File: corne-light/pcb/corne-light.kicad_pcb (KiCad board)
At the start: 2 copper layers, 275.5 x 105.6 mm, 122 parts, among them J1 MJ-4PP-9, J2 OLED, J5 Breakaway_Tabs, J6 MJ-4PP-9, J7 OLED, SW1 SW_PUSH, SW10 SW_PUSH, SW11 SW_PUSH, SW12 SW_PUSH, SW13 SW_PUSH, SW14 SW_PUSH, SW15 SW_PUSH, SW16 SW_PUSH, SW17 SW_PUSH, SW18 SW_PUSH, SW19 SW_PUSH, SW2 SW_PUSH, SW20 SW_PUSH, SW21 SW_PUSH, SW22 SW_PUSH, SW23 SW_PUSH, SW24 SW_PUSH, SW25 SW_PUSH, SW26 SW_PUSH, SW27 SW_PUSH, SW28 SW_PUSH, SW29 SW_PUSH, SW3 SW_PUSH, SW30 SW_PUSH, SW31 SW_PUSH, SW32 SW_PUSH, SW33 SW_PUSH, SW34 SW_PUSH, SW35 SW_PUSH, SW36 SW_PUSH, SW37 SW_PUSH, SW38 SW_PUSH, SW39 SW_PUSH, SW4 SW_PUSH, SW40 SW_PUSH, SW41 SW_PUSH, SW42 SW_PUSH, SW5 SW_PUSH, SW6 SW_PUSH, SW7 SW_PUSH, SW8 SW_PUSH, SW9 SW_PUSH, U1 ProMicro, U2 ProMicro

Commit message: Change switches to redragon ones
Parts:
- removed G*** (x4): LOGO, kbd:corne-logo-horizontal
- removed J1, J6: MJ-4PP-9, kbd:MJ-4PP-9_1side
- removed J5 (x8): Breakaway_Tabs, kbd:Breakaway_Tabs
- removed Ref** (x4): Val**, kbd:thread_m2
- removed Ref** (x14): Val**, kbd:spacer_m2
- D1, D10, D11, D12, D13, D14, D15, D16, D17, D18, D19, D2, D20, D21, D22, D23, D24, D25, D26, D27, D28, D29, D3, D30, D31, D32, D33, D34, D35, D36, D37, D38, D39, D4, D40, D41, D42, D5, D6, D7, D8, D9: footprint kbd:D3_TH_SMD_v2 -> kbd:D3_TH
- SW1, SW10, SW11, SW12, SW13, SW14, SW15, SW16, SW17, SW18, SW19, SW2, SW20, SW22, SW23, SW24, SW25, SW26, SW27, SW28, SW29, SW3, SW30, SW31, SW32, SW33, SW34, SW35, SW36, SW37, SW38, SW39, SW4, SW40, SW41, SW5, SW6, SW7, SW8, SW9: footprint kbd:keyswitch_cherrymx_alps_choc12_1u -> ProjectLocal:SW_Redragon_LowProfile_PCB_1.00u
- SW21, SW42: footprint kbd:keyswitch_cherrymx_alps_choc12_1.5u -> ProjectLocal:SW_Redragon_LowProfile_PCB_1.50u
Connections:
- U1 pad 1: Net-(U1-Pad1) -> unconnected-(U1-TX0/D3-Pad1)
- U1 pad 11: Net-(U1-Pad11) -> unconnected-(U1-8/B4-Pad11)
- U1 pad 12: Net-(U1-Pad12) -> unconnected-(U1-9/B5-Pad12)
- U1 pad 13: Net-(U1-Pad13) -> unconnected-(U1-B6/10-Pad13)
- U1 pad 14: Net-(U1-Pad14) -> unconnected-(U1-B2/16-Pad14)
- U1 pad 2: data -> unconnected-(U1-RX1/D2-Pad2)
- U1 pad 24: Net-(U1-Pad24) -> unconnected-(U1-RAW-Pad24)
- U2 pad 1: Net-(U2-Pad1) -> unconnected-(U2-TX0/D3-Pad1)
- U2 pad 11: Net-(U2-Pad11) -> unconnected-(U2-8/B4-Pad11)
- U2 pad 12: Net-(U2-Pad12) -> unconnected-(U2-9/B5-Pad12)
- U2 pad 13: Net-(U2-Pad13) -> unconnected-(U2-B6/10-Pad13)
- U2 pad 14: Net-(U2-Pad14) -> unconnected-(U2-B2/16-Pad14)
- U2 pad 2: data_r -> unconnected-(U2-RX1/D2-Pad2)
- U2 pad 24: Net-(U2-Pad24) -> unconnected-(U2-RAW-Pad24)
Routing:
- net (no net): track 0.00 -> 528.0 mm
- net unconnected-(U1-RX1/D2-Pad2): track 0.00 -> 78.9 mm
- net data: track 78.9 -> 0.00 mm
- net unconnected-(U2-RX1/D2-Pad2): track 0.00 -> 64.4 mm
- net data_r: track 64.4 -> 0.00 mm
- net Net-(D16-A): track 35.7 -> 0.00 mm
- net Net-(D27-A): track 20.5 -> 6.93 mm
- net Net-(D33-A): track 20.5 -> 6.99 mm
- net Net-(D23-A): track 21.5 -> 8.01 mm
- net Net-(D31-A): track 22.6 -> 9.12 mm
- net Net-(D37-A): track 22.3 -> 8.84 mm
- net Net-(D24-A): track 27.6 -> 14.2 mm
- net Net-(D36-A): track 27.2 -> 13.8 mm
- net Net-(D25-A): track 22.3 -> 8.90 mm
- net Net-(D32-A): track 27.5 -> 14.1 mm
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
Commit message: Change diode orientation on right side
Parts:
- D1, D10, D11, D12, D13, D14, D15, D16, D17, D18, D19, D2, D20, D21, D22, D23, D24, D25, D26, D27, D28, D29, D3, D30, D31, D32, D33, D34, D35, D36, D37, D38, D39, D4, D40, D41, D42, D5, D6, D7, D8, D9: footprint kbd:D3_TH -> Diode_THT:D_DO-35_SOD27_P12.70mm_Horizontal
- moved D42 33.6 mm to (170.8, 84.5), turned to 180 degrees
- moved D24 21.5 mm to (250.5, 53.0)
- moved D30 21.5 mm to (250.5, 72.0)
- moved D36 21.5 mm to (250.5, 91.0)
- moved D26 20.2 mm to (212.0, 51.4)
- moved D32 20.2 mm to (212.0, 70.3)
- moved D38 20.2 mm to (212.0, 89.3)
- moved D27 10.5 mm to (193.0, 51.4)
- moved D33 10.5 mm to (193.0, 70.3)
- moved D39 10.5 mm to (193.0, 89.3)
- moved D37 10.4 mm to (229.7, 89.3)
- moved D25 10.4 mm to (229.7, 51.3)
- moved D31 10.4 mm to (229.7, 70.3)
- moved D40 7.02 mm to (222.0, 92.2), turned to -90 degrees
- moved D41 6.64 mm to (202.0, 92.7), turned to -90 degrees
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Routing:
- net (no net): track 528.0 -> 0.00 mm
- net col0_r: track 183.2 -> 0.00 mm, vias 1 -> 0
- net col0: track 182.3 -> 0.00 mm, vias 1 -> 0
- net row1: track 164.0 -> 0.00 mm
- net col1_r: track 161.3 -> 0.00 mm
- net col1: track 156.5 -> 0.00 mm, vias 1 -> 0
- net row2: track 153.9 -> 0.00 mm
- net col3_r: track 148.5 -> 0.00 mm, vias 1 -> 0
- net row0: track 142.3 -> 0.00 mm
- net col3: track 141.3 -> 0.00 mm, vias 1 -> 0
- net col2_r: track 141.1 -> 0.00 mm, vias 1 -> 0
- net row2_r: track 137.6 -> 0.00 mm, vias 2 -> 0
- net col2: track 135.2 -> 0.00 mm, vias 1 -> 0
- net row1_r: track 134.3 -> 0.00 mm
- net col4_r: track 129.6 -> 0.00 mm, vias 1 -> 0
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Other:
- outline, holes or cut-outs redrawn

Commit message: Route rightside keys
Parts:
- removed D1, D10, D11, D12, D13, D14, D15, D16, D17, D18, D19, D2, D20, D21, D3, D4, D5, D6, D7, D8, D9: D, Diode_THT:D_DO-35_SOD27_P12.70mm_Horizontal
- removed J2, J7: OLED, kbd:OLED_1side
- removed RSW1, RSW2: SW_PUSH, kbd:ResetSW_1side
- removed SW1, SW10, SW11, SW12, SW13, SW14, SW15, SW16, SW17, SW18, SW19, SW2, SW20, SW3, SW4, SW5, SW6, SW7, SW8, SW9: SW_PUSH, ProjectLocal:SW_Redragon_LowProfile_PCB_1.00u
- removed SW21: SW_PUSH, ProjectLocal:SW_Redragon_LowProfile_PCB_1.50u
- removed U2: ProMicro, kbd:ProMicro_v3
- D22, D23, D24, D25, D26, D27, D28, D29, D30, D31, D32, D33, D34, D35, D36, D37, D38, D39, D40, D41, D42: footprint Diode_THT:D_DO-35_SOD27_P12.70mm_Horizontal -> Diode_THT:D_DO-35_SOD27_P10.16mm_Horizontal; moved to F.Cu
- U1: value ProMicro -> nice_nano; footprint kbd:ProMicro_v3 -> PCM_marbastlib-xp-promicroish:nice_nano_AH_USBup
- moved D30 28.4 mm to (231.4, 51.0), turned to 0 degrees
- moved D36 28.0 mm to (230.9, 71.0), turned to 0 degrees
- moved D31 27.5 mm to (212.4, 49.0), turned to 0 degrees
- moved D37 27.4 mm to (211.9, 68.5), turned to 0 degrees
- moved U1 27.2 mm to (164.1, 56.2)
- moved D32 26.5 mm to (193.9, 51.0), turned to 0 degrees
- moved D38 24.8 mm to (195.9, 70.5), turned to 0 degrees
- moved D39 23.1 mm to (179.0, 71.0), turned to 0 degrees
- moved D29 22.4 mm to (250.4, 56.0), turned to 0 degrees
- moved D35 22.1 mm to (250.4, 75.5), turned to 0 degrees
- moved D33 22.0 mm to (179.5, 53.0), turned to 0 degrees
- moved D24 20.5 mm to (231.2, 45.8)
- moved D27 20.4 mm to (175.5, 61.9)
- moved D26 18.2 mm to (194.0, 48.5)
- moved D25 17.9 mm to (212.5, 46.5)
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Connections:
- D22 pad 1: row0_r -> col0_r
- D23 pad 1: row0_r -> col1_r
- D24 pad 1: row0_r -> col2_r
- D25 pad 1: row0_r -> col3_r
- D26 pad 1: row0_r -> col4_r
- D27 pad 1: row0_r -> col5_r
- D28 pad 1: row1_r -> col0_r
- D29 pad 1: row1_r -> col1_r
- D30 pad 1: row1_r -> col2_r
- D31 pad 1: row1_r -> col3_r
- D32 pad 1: row1_r -> col4_r
- D33 pad 1: row1_r -> col5_r
- D34 pad 1: row2_r -> col0_r
- D35 pad 1: row2_r -> col1_r
- D36 pad 1: row2_r -> col2_r
- D37 pad 1: row2_r -> col3_r
- D38 pad 1: row2_r -> col4_r
- D39 pad 1: row2_r -> col5_r
- D40 pad 1: row3_r -> col3_r
- D41 pad 1: row3_r -> col4_r
- D42 pad 1: row3_r -> col5_r
- SW22 pad 1: col0_r -> Net-(D22-A)
- SW22 pad 2: Net-(D22-A) -> row0_r
- SW23 pad 1: col1_r -> Net-(D23-A)
- SW23 pad 2: Net-(D23-A) -> row0_r
- SW24 pad 1: col2_r -> Net-(D24-A)
- SW24 pad 2: Net-(D24-A) -> row0_r
- SW25 pad 1: col3_r -> Net-(D25-A)
- SW25 pad 2: Net-(D25-A) -> row0_r
- SW26 pad 1: col4_r -> Net-(D26-A)
- SW26 pad 2: Net-(D26-A) -> row0_r
- SW27 pad 1: col5_r -> Net-(D27-A)
- SW27 pad 2: Net-(D27-A) -> row0_r
- SW28 pad 1: col0_r -> Net-(D28-A)
- SW28 pad 2: Net-(D28-A) -> row1_r
- SW29 pad 1: col1_r -> Net-(D29-A)
- SW29 pad 2: Net-(D29-A) -> row1_r
- SW30 pad 1: col2_r -> Net-(D30-A)
- SW30 pad 2: Net-(D30-A) -> row1_r
- SW31 pad 1: col3_r -> Net-(D31-A)
- SW31 pad 2: Net-(D31-A) -> row1_r
- SW32 pad 1: col4_r -> Net-(D32-A)
- SW32 pad 2: Net-(D32-A) -> row1_r
- SW33 pad 1: col5_r -> Net-(D33-A)
- SW33 pad 2: Net-(D33-A) -> row1_r
- SW34 pad 1: col0_r -> Net-(D34-A)
- SW34 pad 2: Net-(D34-A) -> row2_r
- SW35 pad 1: col1_r -> Net-(D35-A)
- SW35 pad 2: Net-(D35-A) -> row2_r
- SW36 pad 1: col2_r -> Net-(D36-A)
- SW36 pad 2: Net-(D36-A) -> row2_r
- SW37 pad 1: col3_r -> Net-(D37-A)
- SW37 pad 2: Net-(D37-A) -> row2_r
- SW38 pad 1: col4_r -> Net-(D38-A)
- SW38 pad 2: Net-(D38-A) -> row2_r
- SW39 pad 1: col5_r -> Net-(D39-A)
- SW39 pad 2: Net-(D39-A) -> row2_r
- SW40 pad 1: col3_r -> Net-(D40-A)
- SW40 pad 2: Net-(D40-A) -> row3_r
- SW41 pad 1: col4_r -> Net-(D41-A)
- SW41 pad 2: Net-(D41-A) -> row3_r
- SW42 pad 1: col5_r -> Net-(D42-A)
- SW42 pad 2: Net-(D42-A) -> row3_r
- U1 pad 10: row3 -> col4_r
- U1 pad 11: unconnected-(U1-8/B4-Pad11) -> col3_r
- U1 pad 12: unconnected-(U1-9/B5-Pad12) -> row3_r
- U1 pad 15: col5 -> unconnected-(U1-RST-Pad15)
- U1 pad 16: col4 -> unconnected-(U1-3V3-Pad16)
- U1 pad 17: col3 -> col0_r
- U1 pad 18: col2 -> col1_r
- U1 pad 19: col1 -> col2_r
- U1 pad 20: col0 -> unconnected-(U1-P1.15-LF-Pad20)
- U1 pad 21: VCC -> unconnected-(U1-P1.13-LF-Pad21)
- U1 pad 22: reset -> col5_r
- U1 pad 23: GND -> unconnected-(U1-P0.10-LF-Pad23)
- U1 pad 3: GND -> unconnected-(U1-GND-Pad3)
- U1 pad 4: GND -> unconnected-(U1-GND-Pad4)
- U1 pad 5: SDA -> unconnected-(U1-P0.17-Pad5)
- U1 pad 6: SCL -> unconnected-(U1-P0.20-Pad6)
- U1 pad 7: row0 -> row0_r
- U1 pad 8: row1 -> row1_r
- U1 pad 9: row2 -> row2_r
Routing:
- net row0_r: track 0.00 -> 343.2 mm
- net row2_r: track 0.00 -> 314.3 mm
- net row1_r: track 0.00 -> 286.6 mm
- net col0_r: track 0.00 -> 149.2 mm
- net col3_r: track 0.00 -> 136.1 mm
- net col1_r: track 0.00 -> 124.7 mm
- net col4_r: track 0.00 -> 115.2 mm
- net row3_r: track 0.00 -> 97.9 mm
- net col2_r: track 0.00 -> 92.8 mm
- net col5_r: track 0.00 -> 59.5 mm
- net Net-(D42-A): track 0.00 -> 26.2 mm
- net Net-(D23-A): track 0.00 -> 20.3 mm
- net Net-(D24-A): track 0.00 -> 20.0 mm
- net Net-(D25-A): track 0.00 -> 19.7 mm
- net Net-(D26-A): track 0.00 -> 19.2 mm
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
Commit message: Improve  routing
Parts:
- moved D27 3.48 mm to (175.1, 65.3)
- moved D41 0.98 mm to (195.9, 89.0)
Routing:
- net col2_r: track 92.8 -> 102.2 mm
- net row1_r: track 286.6 -> 292.8 mm
- net col5_r: track 59.5 -> 53.9 mm
- net row0_r: track 343.2 -> 347.4 mm
- net Net-(D27-A): track 14.5 -> 18.1 mm
- net row2_r: track 314.3 -> 316.0 mm
- net Net-(D42-A): track 26.2 -> 27.9 mm
- net row3_r: track 97.9 -> 96.8 mm
- net col4_r: track 115.2 -> 114.5 mm
- net col3_r: track 136.1 -> 135.5 mm
- net col1_r: track 124.7 -> 124.1 mm

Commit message: Improve tracks
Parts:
- D27, D33: footprint Diode_THT:D_DO-35_SOD27_P10.16mm_Horizontal -> Diode_THT:D_DO-35_SOD27_P7.62mm_Horizontal
- moved D25 4.95 mm to (212.2, 51.4)
- moved D26 4.95 mm to (193.7, 53.4)
- moved D31 3.79 mm to (216.2, 48.9)
- moved D32 3.29 mm to (197.2, 51.0)
- moved D33 1.71 mm to (181.2, 53.0)
- moved D27 0.86 mm to (175.1, 64.4)
- moved D37 0.63 mm to (212.2, 67.9)
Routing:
- net row1_r: track 292.8 -> 289.1 mm
- net col2_r: track 102.2 -> 98.9 mm
- net Net-(D26-A): track 19.2 -> 21.5 mm
- net Net-(D25-A): track 19.7 -> 22.0 mm
- net col5_r: track 53.9 -> 55.8 mm
- net row0_r: track 347.4 -> 345.8 mm
- net Net-(D27-A): track 18.1 -> 19.5 mm
- net Net-(D31-A): track 13.8 -> 13.0 mm
- net col0_r: track 149.2 -> 149.9 mm
- net Net-(D32-A): track 14.0 -> 13.3 mm
- net col1_r: track 124.1 -> 124.7 mm

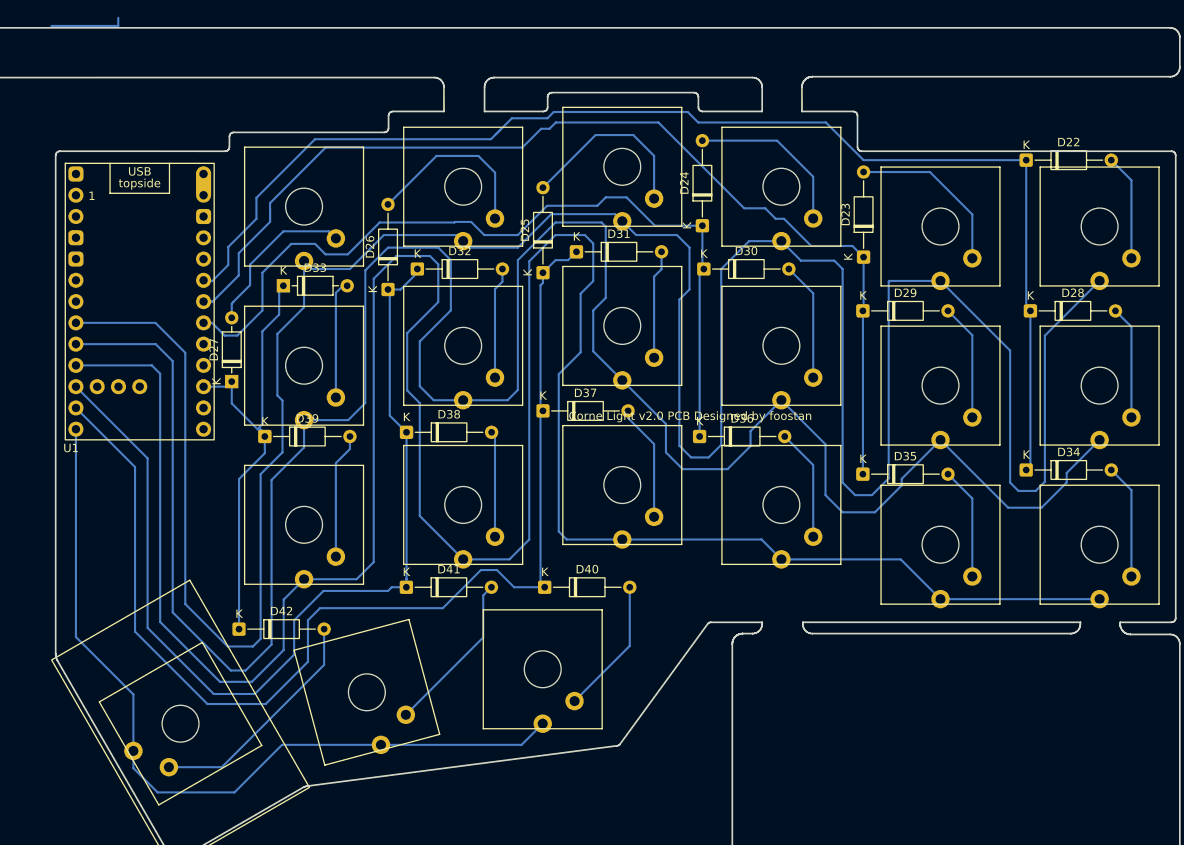
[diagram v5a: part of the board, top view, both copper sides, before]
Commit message: Improve clearances
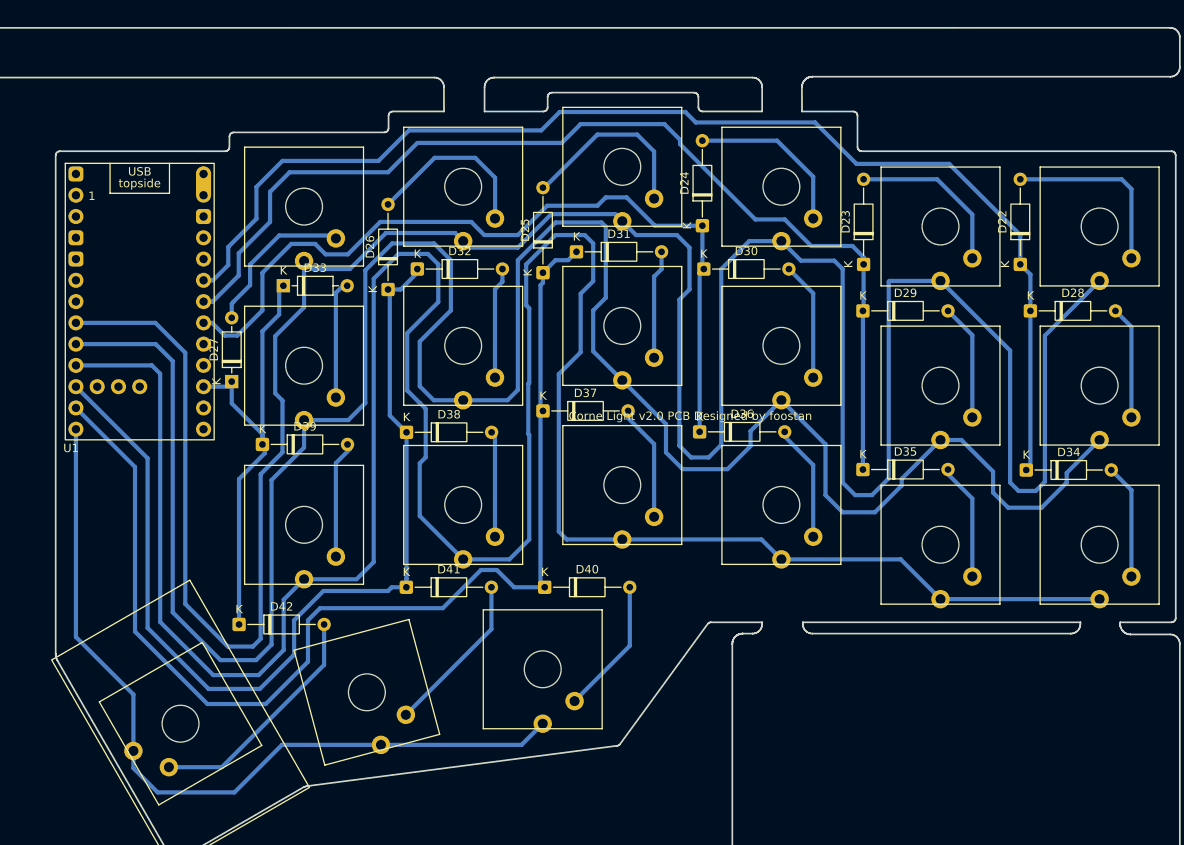
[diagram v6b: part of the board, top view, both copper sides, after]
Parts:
- moved D22 12.5 mm to (269.2, 50.4), turned to 90 degrees
- moved D39 0.99 mm to (178.7, 71.9)
- moved D23 0.87 mm to (250.5, 50.4)
- moved D35 0.56 mm to (250.4, 74.9)
- moved D36 0.56 mm to (230.9, 70.4)
- moved D42 0.56 mm to (175.9, 93.4)
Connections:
- U1 pad 13: unconnected-(U1-BAT+-Pad13) -> Net-(U1-BAT+-Pad13)
- U1 pad 29: unconnected-(U1-BAT+-Pad29) -> Net-(U1-BAT+-Pad13)
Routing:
- net Net-(D22-A): track 12.7 -> 22.0 mm
- net (no net): track 8.98 -> 0.00 mm
- net col0_r: track 149.9 -> 144.9 mm
- net col1_r: track 124.7 -> 123.5 mm
- net row1_r: track 289.1 -> 289.9 mm
- net Net-(D39-A): track 15.0 -> 14.2 mm
- net col2_r: track 98.9 -> 98.3 mm
- net Net-(D42-A): track 27.9 -> 28.4 mm
- net Net-(D36-A): track 13.4 -> 13.9 mm
- net Net-(D35-A): track 13.4 -> 14.0 mm
- net Net-(D26-A): track 21.5 -> 21.0 mm
- net row2_r: track 316.1 -> 316.7 mm
- net col4_r: track 114.5 -> 114.0 mm
